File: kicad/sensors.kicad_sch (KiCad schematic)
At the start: 11 parts, among them U10 BMM350, U11 BMP581, U9 ICM-45686

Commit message: Update repo naming and cleanup files.
Signed-off-by: Benjamin Perseghetti <bperseghetti@rudislabs.com>
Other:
- title: MR-MCXN-T1 Sensor Node -> MR-MCXN-T1
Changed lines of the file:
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@@
 	(paper "A4")
 	(title_block
-		(title "MR-MCXN-T1 Sensor Node")
+		(title "MR-MCXN-T1")
 		(date "2025-03-28")
 		(rev "X0")
 		(company "NXP SEMICONDUCTORS B.V.")
-		(comment 1 "CLASSIFICATION: INTERNAL USE ONLY")
 		(comment 3 "DESIGNER: YOURI TILS")
 		(comment 4 "CTO SYSTEM INNOVATIONS / MOBILE ROBOTICS DOMAIN")
@@
 		)
 		(instances
-			(project "spinali_mcxn_t1_sensor_hub"
+			(project "spinali_mcxn_t1_hub"
 				(path "/8b469ec1-e800-4d46-8a32-95d77ceae6db/a28c0fd8-aeac-4bef-8f3f-cec5db09a131"
 					(reference "#PWR0107")
@@
 		)
 		(instances
-			(project "spinali_mcxn_t1_sensor_hub"
+			(project "spinali_mcxn_t1_hub"
 				(path "/8b469ec1-e800-4d46-8a32-95d77ceae6db/a28c0fd8-aeac-4bef-8f3f-cec5db09a131"
 					(reference "#PWR0118")
@@
 		)
 		(instances
-			(project "spinali_mcxn_t1_sensor_hub"
+			(project "spinali_mcxn_t1_hub"
 				(path "/8b469ec1-e800-4d46-8a32-95d77ceae6db/a28c0fd8-aeac-4bef-8f3f-cec5db09a131"
 					(reference "#PWR0110")
@@
 		)
 		(instances
-			(project "spinali_mcxn_t1_sensor_hub"
+			(project "spinali_mcxn_t1_hub"
 				(path "/8b469ec1-e800-4d46-8a32-95d77ceae6db/a28c0fd8-aeac-4bef-8f3f-cec5db09a131"
 					(reference "C64")
@@
 		)
 		(instances
-			(project "spinali_mcxn_t1_sensor_hub"
+			(project "spinali_mcxn_t1_hub"
 				(path "/8b469ec1-e800-4d46-8a32-95d77ceae6db/a28c0fd8-aeac-4bef-8f3f-cec5db09a131"
 					(reference "C63")
@@
 		)
 		(instances
-			(project "spinali_mcxn_t1_sensor_hub"
+			(project "spinali_mcxn_t1_hub"
 				(path "/8b469ec1-e800-4d46-8a32-95d77ceae6db/a28c0fd8-aeac-4bef-8f3f-cec5db09a131"
 					(reference "C61")
@@
 		)
 		(instances
-			(project "spinali_mcxn_t1_sensor_hub"
+			(project "spinali_mcxn_t1_hub"
 				(path "/8b469ec1-e800-4d46-8a32-95d77ceae6db/a28c0fd8-aeac-4bef-8f3f-cec5db09a131"
 					(reference "#PWR0115")
@@
 		)
 		(instances
-			(project "spinali_mcxn_t1_sensor_hub"
+			(project "spinali_mcxn_t1_hub"
 				(path "/8b469ec1-e800-4d46-8a32-95d77ceae6db/a28c0fd8-aeac-4bef-8f3f-cec5db09a131"
 					(reference "#PWR0108")
@@
 		)
 		(instances
-			(project "spinali_mcxn_t1_sensor_hub"
+			(project "spinali_mcxn_t1_hub"
 				(path "/8b469ec1-e800-4d46-8a32-95d77ceae6db/a28c0fd8-aeac-4bef-8f3f-cec5db09a131"
 					(reference "#PWR0116")
@@
 		)
 		(instances
-			(project "spinali_mcxn_t1_sensor_hub"
+			(project "spinali_mcxn_t1_hub"
 				(path "/8b469ec1-e800-4d46-8a32-95d77ceae6db/a28c0fd8-aeac-4bef-8f3f-cec5db09a131"
 					(reference "C65")
@@
 		)
 		(instances
-			(project "spinali_mcxn_t1_sensor_hub"
+			(project "spinali_mcxn_t1_hub"
 				(path "/8b469ec1-e800-4d46-8a32-95d77ceae6db/a28c0fd8-aeac-4bef-8f3f-cec5db09a131"
 					(reference "#PWR0119")
@@
 		)
 		(instances
-			(project "spinali_mcxn_t1_sensor_hub"
+			(project "spinali_mcxn_t1_hub"
 				(path "/8b469ec1-e800-4d46-8a32-95d77ceae6db/a28c0fd8-aeac-4bef-8f3f-cec5db09a131"
 					(reference "#PWR0123")
@@
 		)
 		(instances
-			(project "spinali_mcxn_t1_sensor_hub"
+			(project "spinali_mcxn_t1_hub"
 				(path "/8b469ec1-e800-4d46-8a32-95d77ceae6db/a28c0fd8-aeac-4bef-8f3f-cec5db09a131"
 					(reference "#PWR0106")
@@
 		)
 		(instances
-			(project "spinali_mcxn_t1_sensor_hub"
+			(project "spinali_mcxn_t1_hub"
 				(path "/8b469ec1-e800-4d46-8a32-95d77ceae6db/a28c0fd8-aeac-4bef-8f3f-cec5db09a131"
 					(reference "#PWR0112")
@@
 		)
 		(instances
-			(project "spinali_mcxn_t1_sensor_hub"
+			(project "spinali_mcxn_t1_hub"
 				(path "/8b469ec1-e800-4d46-8a32-95d77ceae6db/a28c0fd8-aeac-4bef-8f3f-cec5db09a131"
 					(reference "#PWR0125")
@@
 		)
 		(instances
-			(project "spinali_mcxn_t1_sensor_hub"
+			(project "spinali_mcxn_t1_hub"
 				(path "/8b469ec1-e800-4d46-8a32-95d77ceae6db/a28c0fd8-aeac-4bef-8f3f-cec5db09a131"
 					(reference "#PWR0117")
@@
 		)
 		(instances
-			(project "spinali_mcxn_t1_sensor_hub"
+			(project "spinali_mcxn_t1_hub"
 				(path "/8b469ec1-e800-4d46-8a32-95d77ceae6db/a28c0fd8-aeac-4bef-8f3f-cec5db09a131"
 					(reference "#PWR0114")
@@
 		)
 		(instances
-			(project "spinali_mcxn_t1_sensor_hub"
+			(project "spinali_mcxn_t1_hub"
 				(path "/8b469ec1-e800-4d46-8a32-95d77ceae6db/a28c0fd8-aeac-4bef-8f3f-cec5db09a131"
 					(reference "C62")
@@
 		)
 		(instances
-			(project "spinali_mcxn_t1_sensor_hub"
+			(project "spinali_mcxn_t1_hub"
 				(path "/8b469ec1-e800-4d46-8a32-95d77ceae6db/a28c0fd8-aeac-4bef-8f3f-cec5db09a131"
 					(reference "#PWR0111")
@@
 		)
 		(instances
-			(project "spinali_mcxn_t1_sensor_hub"
+			(project "spinali_mcxn_t1_hub"
 				(path "/8b469ec1-e800-4d46-8a32-95d77ceae6db/a28c0fd8-aeac-4bef-8f3f-cec5db09a131"
 					(reference "#PWR0120")
@@
 		)
 		(instances
-			(project "spinali_mcxn_t1_sensor_hub"
+			(project "spinali_mcxn_t1_hub"
 				(path "/8b469ec1-e800-4d46-8a32-95d77ceae6db/a28c0fd8-aeac-4bef-8f3f-cec5db09a131"
 					(reference "C60")

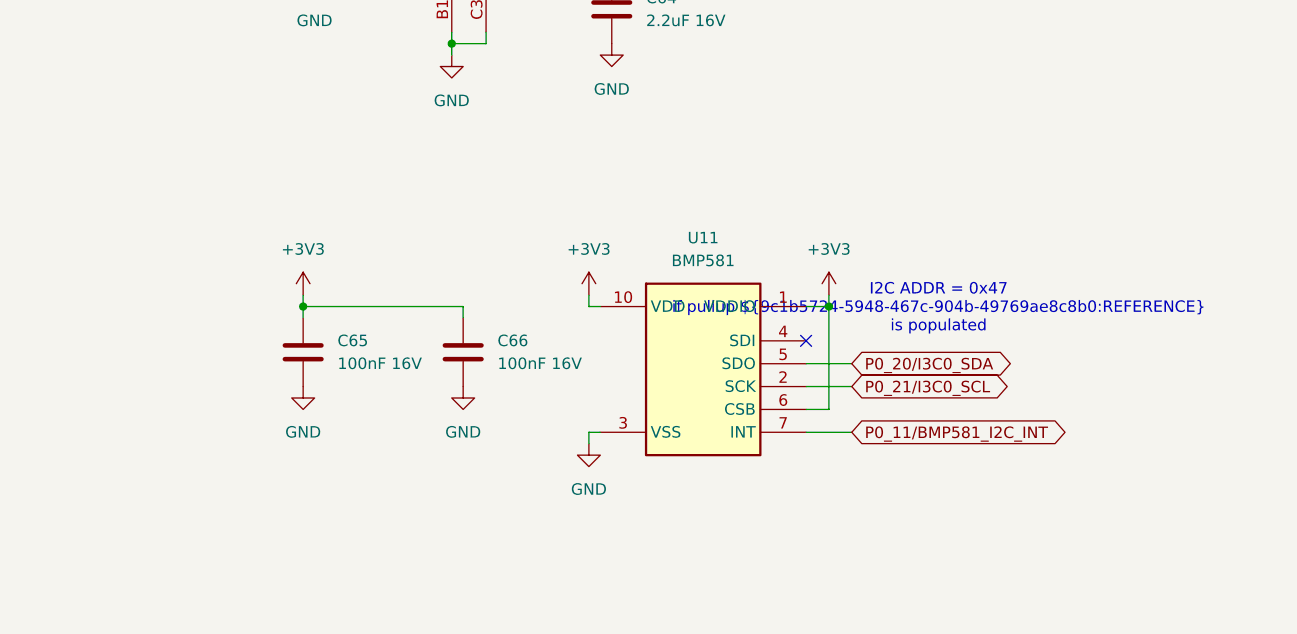
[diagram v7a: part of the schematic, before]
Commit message: Patched schematic and board layout
- Replaced choke in series with Vbus with 2A choke.
- Fixed interface to the BMP581 barometer.
- Added schematic fixes to the layout.
- Completed DRC.
- Created production folder with Gerber, BOM, positions and schematic.
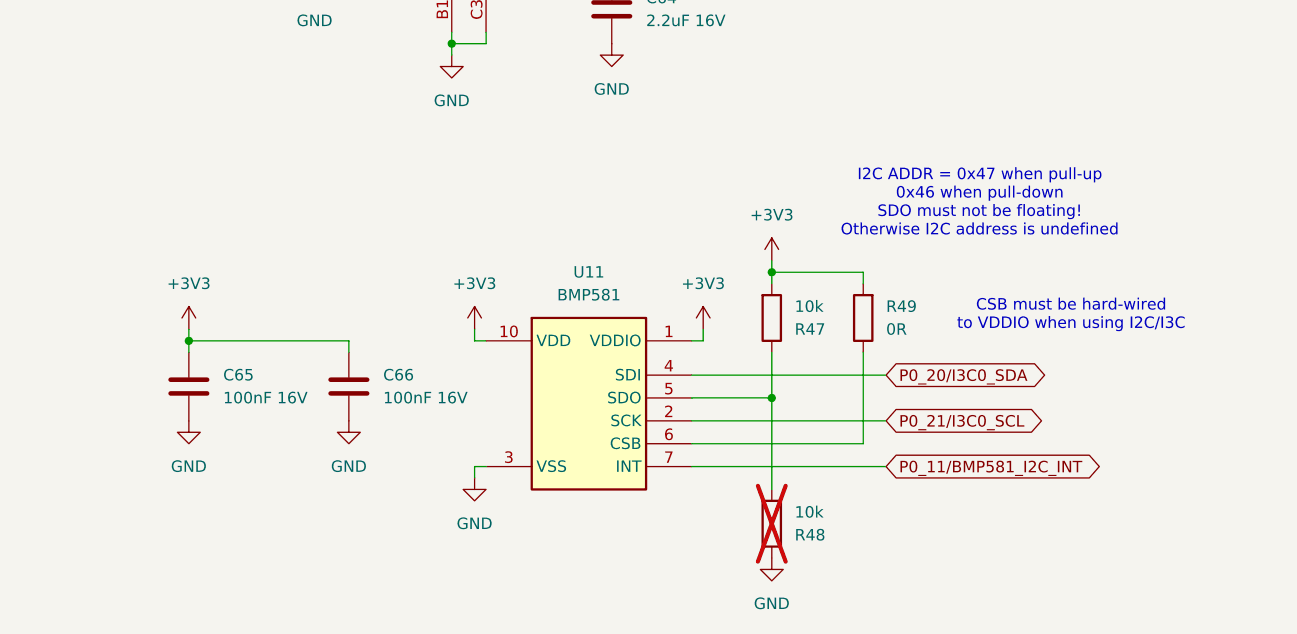
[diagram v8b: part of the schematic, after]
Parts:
- added R47, R48: 10k, Resistor_SMD:R_0402_1005Metric, symbol Device:R
- added R49: 0R, Resistor_SMD:R_0402_1005Metric, symbol Device:R
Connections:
- net +3V3: now also R47.2, R49.2; no longer U11.6 (CSB)
- net GND: now also R48.1
- net P0_20/I3C0_SDA: now also U11.4 (SDI); no longer U11.5 (SDO)
- new net: R47.1, R48.2, U11.5 (SDO)
- new net: R49.1, U11.6 (CSB)
- no-connect marks 5 -> 4
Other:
- note added: "CSB must be hard-wired to VDDIO when using I2C/I3C"
- note added: "I2C ADDR = 0x47 when pull-up 0x46 when pull-down SDO must not be floating! Otherwise I2C address is undefined"
- note removed: "I2C ADDR = 0x47 if pullup ${9c1b5724-5948-467c-904b-49769ae8c8b0:REFERENCE} is populated"
- moved on the sheet: C65, C66, U11
